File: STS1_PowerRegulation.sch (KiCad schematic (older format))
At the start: 20 parts, among them U2 LT3120

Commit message: schematic done
final tweaks (adding LEDS, pin headers, moving circuits...)
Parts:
- added C27, C29, C30: 10u, symbol Device:C
- added C28: 0.001u, symbol Device:C
- added R12: 100k, symbol Device:R
- R10: value 316k -> 321k
- R9: value 100k -> 10k
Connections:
- net VCC_INT is gone; now on net V_out: R9.1
- net GND: now also C27.2, C28.2, C29.2, C30.2
- net Pgood: now also C28.1, R12.1; no longer R9.2, U2.~ (Vin)
- net V_out: now also C27.1, C29.1, C30.1
- new net: R12.2, R9.2, U2.~ (Vin)
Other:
- moved on the sheet: C17, C18, C19, C20, C21, C22, C23, C24, C25, C26, D4, L1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

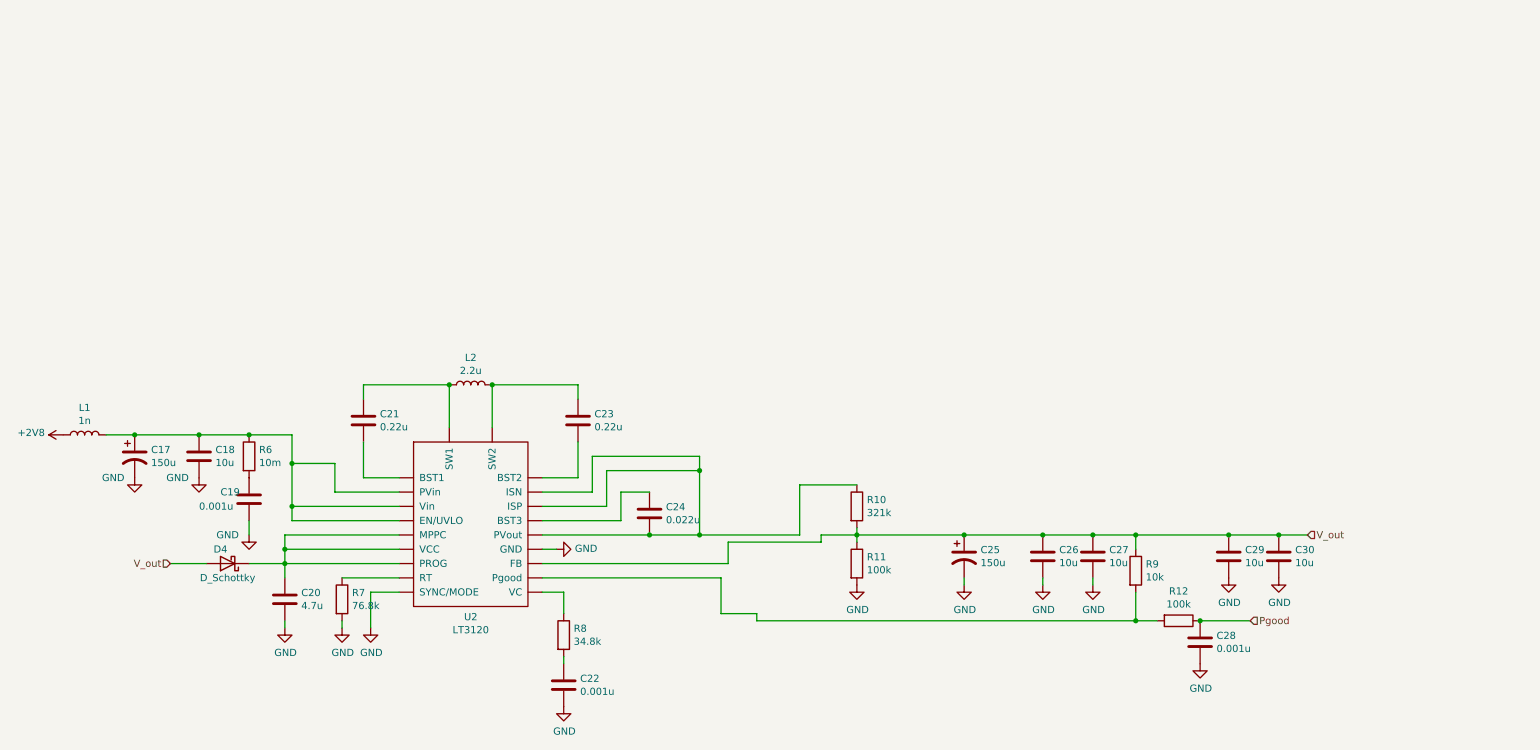
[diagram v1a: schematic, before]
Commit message: Issues removed + further layout development
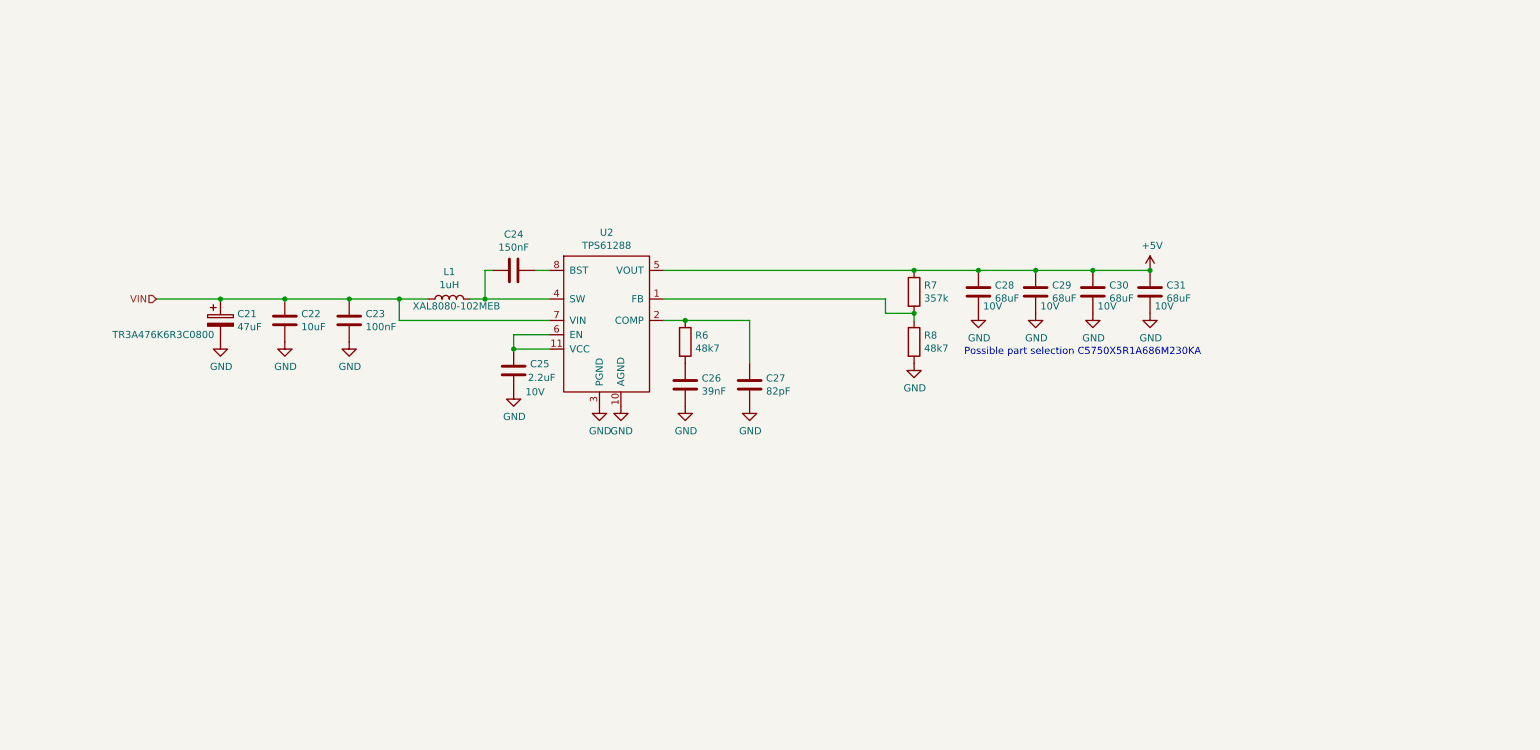
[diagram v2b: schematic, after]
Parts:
- removed C17, C25: 150u, symbol Device:CP1
- removed C18: 10u, symbol Device:C
- removed C19: 0.001u, symbol Device:C
- removed C20: 4.7u, symbol Device:C
- removed C21: 0.22u, symbol Device:C
- removed D4: D_Schottky, symbol Device:D_Schottky
- removed L2: 2.2u, symbol Device:L
- removed R10: 321k, symbol Device:R
- removed R11, R12: 100k, symbol Device:R
- removed R9: 10k, symbol Device:R
- removed U2: LT3120, symbol STS1BuckBoost:LT3120
- added C21: 47uF, Capacitor_Tantalum_SMD:CP_EIA-3216-18_Kemet-A, symbol Device:CP
- added C25: 2.2uF, Capacitor_SMD:C_0603_1608Metric, symbol Device:C
- added C31: 68uF, Capacitor_SMD:C_2220_5650Metric, symbol Device:C
- added U2: TPS61288, STS1_DCDC:VQFN-HR, symbol STS1_DCDC:TPS61288
- C22: value 0.001u -> 10uF; footprint (none) -> Capacitor_SMD:C_1206_3216Metric
- C23: value 0.22u -> 100nF; footprint (none) -> Capacitor_SMD:C_0603_1608Metric
- C24: value 0.022u -> 150nF; footprint (none) -> Capacitor_SMD:C_0603_1608Metric
- C26: value 10u -> 39nF; footprint (none) -> Capacitor_SMD:C_0603_1608Metric
- C27: value 10u -> 82pF; footprint (none) -> Capacitor_SMD:C_0603_1608Metric
- C28: value 0.001u -> 68uF; footprint (none) -> Capacitor_SMD:C_2220_5650Metric; Part (none) -> C5750X5R1A686M230KA; Voltage (none) -> 10V
- C29, C30: value 10u -> 68uF; footprint (none) -> Capacitor_SMD:C_2220_5650Metric; Part (none) -> C5750X5R1A686M230KA; Voltage (none) -> 10V
- L1: value 1n -> 1uH; footprint (none) -> STS1_DCDC:XAL8080; Part (none) -> XAL8080-102MEB
- R6: value 10m -> 48k7; footprint (none) -> Resistor_SMD:R_0603_1608Metric
- R7: value 76.8k -> 357k; footprint (none) -> Resistor_SMD:R_0603_1608Metric
- R8: value 34.8k -> 48k7; footprint (none) -> Resistor_SMD:R_0603_1608Metric
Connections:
- net +2V8 is gone; now on net VIN: L1.1
- net Pgood is gone; now on net +5V: C28.1
- net GND: now also C23.2, R8.2, C21.2, C25.2, C31.2, U2.10 (AGND), U2.3 (PGND); no longer R7.2
- net VIN: now reaches C23.1
- net VIN: now also C22.1, C21.1, U2.7 (VIN)
- net at C24.1: now also U2.8 (BST)
- net at C24.2: now also L1.2, U2.4 (SW), U2.9 (SW)
- net at R8.1: now also R7.2, U2.1 (FB)
- net +5V: now reaches R7.1
- net +5V: now also C29.1, C30.1, C31.1, U2.5 (VOUT)
- net at R6.1: now also C27.1, U2.2 (COMP); no longer L1.2
- net at R6.2: now also C26.1
- removed net V_out: C26.1, C27.1, C29.1, C30.1
- new net: C25.1, U2.11 (VCC), U2.6 (EN)
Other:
- note added: "Possible part selection C5750X5R1A686M230KA"

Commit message: final version1
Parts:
- added C33, C35: 4.7µF, Capacitor_SMD:C_0805_2012Metric, symbol Device:C
- added C34: 0.1µ, Capacitor_SMD:C_0805_2012Metric, symbol Device:C
- added D4: LED, LED_SMD:LED_0805_2012Metric, symbol Device:LED
- added R9: 1k, Resistor_SMD:R_0805_2012Metric, symbol Device:R
- added U3: MCP1725-3302E_MC, STS1_3V3:MCP1725-3302E&slash_MC, symbol STS1_3V3:MCP1725-3302E_MC
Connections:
- net +5V: now also C33.2, U3.1 (VIN), U3.2 (VIN), U3.3 (*SHDN)
- net GND: now also C33.1, C34.2, C35.1, D4.1 (K), U3.4 (GND), U3.9 (EP)
- new net: C34.1, U3.6 (CDELAY)
- new net: R9.1, U3.5 (PWRGD)
- new net: D4.2 (A), R9.2
- new net +3V3: C35.2, U3.7 (SENSE), U3.8 (VOUT)
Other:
- note added: "Kerko\n"
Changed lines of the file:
@@
 $Descr A4 11693 8268
 encoding utf-8
-Sheet 5 5
+Sheet 4 6
 Title ""
 Date ""
@@
 Text Notes 7700 3200 0    50   ~ 0
 Possible part selection C5750X5R1A686M230KA
+$Comp
+L STS1_3V3:MCP1725-3302E_MC U3
+U 1 1 6199338A
+P 8900 1400
+F 0 "U3" H 9900 1787 60  0000 C CNN
+F 1 "MCP1725-3302E_MC" H 9900 1681 60  0000 C CNN
+F 2 "STS1_3V3:MCP1725-3302E&slash_MC" H 9900 1640 60  0001 C CNN
+F 3 "https://www.farnell.com/datasheets/808903.pdf" H 9850 1950 60  0000 C CNN
+	1    8900 1400
+	1    0    0    -1
+$EndComp
+Wire Wire Line
+	9000 2600 9200 2600
+Wire Wire Line
+	9200 2600 9200 2250
+Wire Wire Line
+	9200 2250 8700 2250
+Wire Wire Line
+	8500 2250 8500 1400
+Wire Wire Line
+	8500 1400 8750 1400
+$Comp
+L Device:C C33
+U 1 1 61995988
+P 8750 1250
+F 0 "C33" H 8865 1296 50  0000 L CNN
+F 1 "4.7µF" H 8400 1250 50  0000 L CNN
+F 2 "Capacitor_SMD:C_0805_2012Metric" H 8788 1100 50  0001 C CNN
+F 3 "~" H 8750 1250 50  0001 C CNN
+	1    8750 1250
+	1    0    0    -1
+$EndComp
+Connection ~ 8750 1400
+Wire Wire Line
+	8750 1400 8900 1400
+$Comp
+L power:GND #PWR023
+U 1 1 619967E2
+P 8600 950
+F 0 "#PWR023" H 8600 700 50  0001 C CNN
+F 1 "GND" H 8605 777 50  0000 C CNN
+F 2 "" H 8600 950 50  0001 C CNN
+F 3 "" H 8600 950 50  0001 C CNN
+	1    8600 950
+	1    0    0    -1
+$EndComp
+Wire Wire Line
+	8750 1100 8750 900
+Wire Wire Line
+	8750 900  8600 900
+Wire Wire Line
+	8600 900  8600 950
+Wire Wire Line
+	8750 1400 8750 1500
+Wire Wire Line
+	8750 1500 8900 1500
+Wire Wire Line
+	8700 2250 8700 1600
+Wire Wire Line
+	8700 1600 8900 1600
+Connection ~ 8700 2250
+Wire Wire Line
+	8700 2250 8500 2250
+$Comp
+L power:GND #PWR024
+U 1 1 61999442
+P 8850 1750
+F 0 "#PWR024" H 8850 1500 50  0001 C CNN
+F 1 "GND" H 8855 1577 50  0000 C CNN
+F 2 "" H 8850 1750 50  0001 C CNN
+F 3 "" H 8850 1750 50  0001 C CNN
+	1    8850 1750
+	1    0    0    -1
+$EndComp
+Wire Wire Line
+	8900 1700 8850 1700
+Wire Wire Line
+	8850 1700 8850 1750
+Wire Wire Line
+	10900 1600 11150 1600
+Wire Wire Line
+	11150 1600 11150 1500
+Wire Wire Line
+	11150 1500 11100 1500
+$Comp
+L Device:C C35
+U 1 1 619A5F9B
+P 11100 1350
+F 0 "C35" H 11150 1450 50  0000 L CNN
+F 1 "4.7µF" H 11100 1250 50  0000 L CNN
+F 2 "Capacitor_SMD:C_0805_2012Metric" H 11138 1200 50  0001 C CNN
+F 3 "~" H 11100 1350 50  0001 C CNN
+	1    11100 1350
+	1    0    0    -1
+$EndComp
+Connection ~ 11100 1500
+Wire Wire Line
+	11100 1500 10950 1500
+$Comp
+L power:GND #PWR027
+U 1 1 619A6A54
+P 11000 1100
+F 0 "#PWR027" H 11000 850 50  0001 C CNN
+F 1 "GND" H 11005 927 50  0000 C CNN
+F 2 "" H 11000 1100 50  0001 C CNN
+F 3 "" H 11000 1100 50  0001 C CNN
+	1    11000 1100
+	1    0    0    -1
+$EndComp
+Wire Wire Line
+	11100 1200 11100 1000
+Wire Wire Line
+	11100 1000 11000 1000
+Wire Wire Line
+	11000 1000 11000 1100
+Text Notes 11100 1200 0    50   ~ 0
+Kerko\n
+$Comp
+L Device:C C34
+U 1 1 6197D6D8
+P 11050 2100
+F 0 "C34" H 11165 2146 50  0000 L CNN
+F 1 "0.1µ" H 10700 2100 50  0000 L CNN
+F 2 "Capacitor_SMD:C_0805_2012Metric" H 11088 1950 50  0001 C CNN
+F 3 "~" H 11050 2100 50  0001 C CNN
+	1    11050 2100
+	1    0    0    -1
+$EndComp
+$Comp
+L power:GND #PWR028
+U 1 1 6197E02C
+P 11050 2250
+F 0 "#PWR028" H 11050 2000 50  0001 C CNN
+F 1 "GND" H 11055 2077 50  0000 C CNN
+F 2 "" H 11050 2250 50  0001 C CNN
+F 3 "" H 11050 2250 50  0001 C CNN
+	1    11050 2250
+	1    0    0    -1
+$EndComp
+Wire Wire Line
+	10900 1700 11050 1700
+Wire Wire Line
+	11050 1700 11050 1950
+$Comp
+L Device:R R9
+U 1 1 6197F7C2
+P 10550 2300
+F 0 "R9" H 10620 2346 50  0000 L CNN
+F 1 "1k" H 10620 2255 50  0000 L CNN
+F 2 "Resistor_SMD:R_0805_2012Metric" V 10480 2300 50  0001 C CNN
+F 3 "~" H 10550 2300 50  0001 C CNN
+	1    10550 2300
+	1    0    0    -1
+$EndComp
+Wire Wire Line
+	10550 2150 10550 2050
+Wire Wire Line
+	10550 2050 10900 2050
+Wire Wire Line
+	10900 2050 10900 1800
+$Comp
+L power:GND #PWR025
+U 1 1 6198107B
+P 10550 2750
+F 0 "#PWR025" H 10550 2500 50  0001 C CNN
+F 1 "GND" H 10555 2577 50  0000 C CNN
+F 2 "" H 10550 2750 50  0001 C CNN
+F 3 "" H 10550 2750 50  0001 C CNN
+	1    10550 2750
+	1    0    0    -1
+$EndComp
+$Comp
+L Device:LED D4
+U 1 1 61981BA6
+P 10550 2600
+F 0 "D4" V 10589 2482 50  0000 R CNN
+F 1 "LED" V 10498 2482 50  0000 R CNN
+F 2 "LED_SMD:LED_0805_2012Metric" H 10550 2600 50  0001 C CNN
+F 3 "~" H 10550 2600 50  0001 C CNN
+	1    10550 2600
+	0    -1   -1   0
+$EndComp
+Text Notes 8750 1150 0    50   ~ 0
+Kerko\n
+Text Notes 11150 2200 0    50   ~ 0
+Kerko\n
+$Comp
+L power:+3V3 #PWR026
+U 1 1 619903E6
+P 10950 1500
+F 0 "#PWR026" H 10950 1350 50  0001 C CNN
+F 1 "+3V3" H 10800 1550 50  0000 C CNN
+F 2 "" H 10950 1500 50  0001 C CNN
+F 3 "" H 10950 1500 50  0001 C CNN
+	1    10950 1500
+	1    0    0    -1
+$EndComp
+Connection ~ 10950 1500
+Wire Wire Line
+	10950 1500 10900 1500
+$Comp
+L power:GND #PWR0138
+U 1 1 61993623
+P 10900 1400
+F 0 "#PWR0138" H 10900 1150 50  0001 C CNN
+F 1 "GND" H 11000 1250 50  0000 C CNN
+F 2 "" H 10900 1400 50  0001 C CNN
+F 3 "" H 10900 1400 50  0001 C CNN
+	1    10900 1400
+	-1   0    0    1
+$EndComp
 $EndSCHEMATC

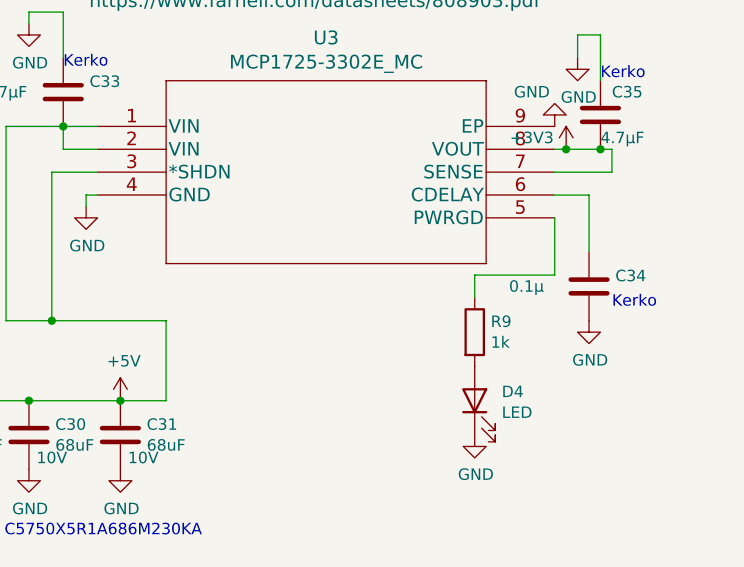
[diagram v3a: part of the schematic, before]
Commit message: added powerplane + testpoints + some debugging
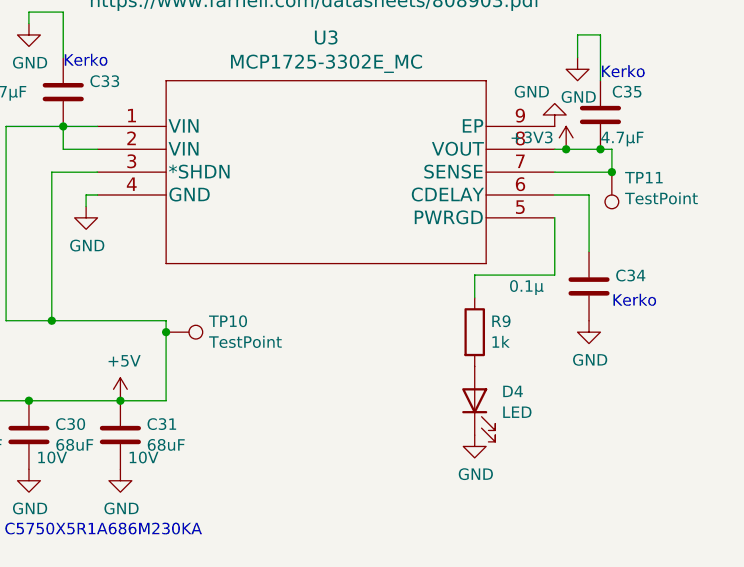
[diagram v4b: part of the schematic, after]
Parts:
- added TP10, TP11: TestPoint, STS1library:STS1_Testpoint, symbol Connector:TestPoint
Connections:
- net +3V3: now also TP11.1
- net +5V: now also TP10.1
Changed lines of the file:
@@
 	9000 2600 9200 2600
 Wire Wire Line
-	9200 2600 9200 2250
+	9200 2600 9200 2300
 Wire Wire Line
 	9200 2250 8700 2250
@@
 	-1   0    0    1
 $EndComp
+$Comp
+L Connector:TestPoint TP11
+U 1 1 61B6866A
+P 11150 1600
+F 0 "TP11" H 11092 1626 50  0000 R CNN
+F 1 "TestPoint" H 11092 1717 50  0000 R CNN
+F 2 "STS1library:STS1_Testpoint" H 11350 1600 50  0001 C CNN
+F 3 "~" H 11350 1600 50  0001 C CNN
+	1    11150 1600
+	-1   0    0    1
+$EndComp
+Connection ~ 11150 1600
+$Comp
+L Connector:TestPoint TP10
+U 1 1 61B68D6F
+P 9200 2300
+F 0 "TP10" V 9154 2488 50  0000 L CNN
+F 1 "TestPoint" V 9245 2488 50  0000 L CNN
+F 2 "STS1library:STS1_Testpoint" H 9400 2300 50  0001 C CNN
+F 3 "~" H 9400 2300 50  0001 C CNN
+	1    9200 2300
+	0    1    1    0
+$EndComp
+Connection ~ 9200 2300
+Wire Wire Line
+	9200 2300 9200 2250
 $EndSCHEMATC

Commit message: finished prototype
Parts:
- C21: value 47uF -> 47u
- C22: value 10uF -> 10u
- C23: value 100nF -> 100n
- C24: value 150nF -> 150n
- C25: value 2.2uF -> 2.2u
- C26: value 39nF -> 39n
- C27: value 82pF -> 82p
- C28, C29, C30, C31: value 68uF -> 68u
- C33, C35: value 4.7µF -> 4.7u
- C34: value 0.1µ -> 0.1u
- L1: value 1uH -> 1u
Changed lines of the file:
@@
 P 4550 3300
 F 0 "C25" H 4665 3346 50  0000 L CNN
-F 1 "2.2uF" H 4650 3250 50  0000 L CNN
+F 1 "2.2u" H 4650 3250 50  0000 L CNN
 F 2 "Capacitor_SMD:C_0603_1608Metric" H 4588 3150 50  0001 C CNN
 F 3 "~" H 4550 3300 50  0001 C CNN
@@
 P 4100 2800
 F 0 "L1" V 4290 2800 50  0000 C CNN
-F 1 "1uH" V 4199 2800 50  0000 C CNN
+F 1 "1u" V 4199 2800 50  0000 C CNN
 F 2 "STS1_DCDC:XAL8080" H 4100 2800 50  0001 C CNN
 F 3 "~" H 4100 2800 50  0001 C CNN
@@
 P 4550 2600
 F 0 "C24" V 4298 2600 50  0000 C CNN
-F 1 "150nF" V 4389 2600 50  0000 C CNN
+F 1 "150n" V 4389 2600 50  0000 C CNN
 F 2 "Capacitor_SMD:C_0603_1608Metric" H 4588 2450 50  0001 C CNN
 F 3 "~" H 4550 2600 50  0001 C CNN
@@
 P 3400 2950
 F 0 "C23" H 3515 2996 50  0000 L CNN
-F 1 "100nF" H 3515 2905 50  0000 L CNN
+F 1 "100n" H 3515 2905 50  0000 L CNN
 F 2 "Capacitor_SMD:C_0603_1608Metric" H 3438 2800 50  0001 C CNN
 F 3 "~" H 3400 2950 50  0001 C CNN
@@
 P 2950 2950
 F 0 "C22" H 3065 2996 50  0000 L CNN
-F 1 "10uF" H 3065 2905 50  0000 L CNN
+F 1 "10u" H 3065 2905 50  0000 L CNN
 F 2 "Capacitor_SMD:C_1206_3216Metric" H 2988 2800 50  0001 C CNN
 F 3 "~" H 2950 2950 50  0001 C CNN
@@
 P 2500 2950
 F 0 "C21" H 2618 2996 50  0000 L CNN
-F 1 "47uF" H 2618 2905 50  0000 L CNN
+F 1 "47u" H 2618 2905 50  0000 L CNN
 F 2 "Capacitor_Tantalum_SMD:CP_EIA-3216-18_Kemet-A" H 2538 2800 50  0001 C CNN
 F 3 "~" H 2500 2950 50  0001 C CNN
@@
 P 5750 3400
 F 0 "C26" H 5865 3446 50  0000 L CNN
-F 1 "39nF" H 5865 3355 50  0000 L CNN
+F 1 "39n" H 5865 3355 50  0000 L CNN
 F 2 "Capacitor_SMD:C_0603_1608Metric" H 5788 3250 50  0001 C CNN
 F 3 "~" H 5750 3400 50  0001 C CNN
@@
 P 6200 3400
 F 0 "C27" H 6315 3446 50  0000 L CNN
-F 1 "82pF" H 6315 3355 50  0000 L CNN
+F 1 "82p" H 6315 3355 50  0000 L CNN
 F 2 "Capacitor_SMD:C_0603_1608Metric" H 6238 3250 50  0001 C CNN
 F 3 "~" H 6200 3400 50  0001 C CNN
@@
 P 7800 2750
 F 0 "C28" H 7915 2796 50  0000 L CNN
-F 1 "68uF" H 7915 2705 50  0000 L CNN
+F 1 "68u" H 7915 2705 50  0000 L CNN
 F 2 "Capacitor_SMD:C_2220_5650Metric" H 7838 2600 50  0001 C CNN
 F 3 "~" H 7800 2750 50  0001 C CNN
@@
 P 8200 2750
 F 0 "C29" H 8315 2796 50  0000 L CNN
-F 1 "68uF" H 8315 2705 50  0000 L CNN
+F 1 "68u" H 8315 2705 50  0000 L CNN
 F 2 "Capacitor_SMD:C_2220_5650Metric" H 8238 2600 50  0001 C CNN
 F 3 "~" H 8200 2750 50  0001 C CNN
@@
 P 8600 2750
 F 0 "C30" H 8715 2796 50  0000 L CNN
-F 1 "68uF" H 8715 2705 50  0000 L CNN
+F 1 "68u" H 8715 2705 50  0000 L CNN
 F 2 "Capacitor_SMD:C_2220_5650Metric" H 8638 2600 50  0001 C CNN
 F 3 "~" H 8600 2750 50  0001 C CNN
@@
 P 9000 2750
 F 0 "C31" H 9115 2796 50  0000 L CNN
-F 1 "68uF" H 9115 2705 50  0000 L CNN
+F 1 "68u" H 9115 2705 50  0000 L CNN
 F 2 "Capacitor_SMD:C_2220_5650Metric" H 9038 2600 50  0001 C CNN
 F 3 "~" H 9000 2750 50  0001 C CNN
@@
 P 8750 1250
 F 0 "C33" H 8865 1296 50  0000 L CNN
-F 1 "4.7µF" H 8400 1250 50  0000 L CNN
+F 1 "4.7u" H 8400 1250 50  0000 L CNN
 F 2 "Capacitor_SMD:C_0805_2012Metric" H 8788 1100 50  0001 C CNN
 F 3 "~" H 8750 1250 50  0001 C CNN
@@
 P 11100 1350
 F 0 "C35" H 11150 1450 50  0000 L CNN
-F 1 "4.7µF" H 11100 1250 50  0000 L CNN
+F 1 "4.7u" H 11100 1250 50  0000 L CNN
 F 2 "Capacitor_SMD:C_0805_2012Metric" H 11138 1200 50  0001 C CNN
 F 3 "~" H 11100 1350 50  0001 C CNN
@@
 P 11050 2100
 F 0 "C34" H 11165 2146 50  0000 L CNN
-F 1 "0.1µ" H 10700 2100 50  0000 L CNN
+F 1 "0.1u" H 10850 2050 50  0000 L CNN
 F 2 "Capacitor_SMD:C_0805_2012Metric" H 11088 1950 50  0001 C CNN
 F 3 "~" H 11050 2100 50  0001 C CNN
